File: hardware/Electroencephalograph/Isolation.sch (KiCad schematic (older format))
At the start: 17 parts, among them U4 THI3-0511, U5 ADUM2401BRWZ

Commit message: further routing
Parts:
- added TP14, TP15, TP16, TP8: TestPoint, TestPoint:TestPoint_Pad_D1.0mm, symbol Connector:TestPoint
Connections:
- net CS: now also TP14.1
- net MISO: now also TP8.1
- net MOSI: now also TP15.1
- net SCK: now also TP16.1
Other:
- moved on the sheet: C51
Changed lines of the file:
@@
 Wire Wire Line
 	3100 2600 3100 3200
-Text GLabel 1750 2700 0    50   Input ~ 0
+Text GLabel 1150 2700 0    50   Input ~ 0
 SCK
-Text GLabel 1750 2800 0    50   Input ~ 0
+Text GLabel 1150 2800 0    50   Input ~ 0
 MOSI
-Text GLabel 1750 2900 0    50   Input ~ 0
+Text GLabel 1150 2900 0    50   Input ~ 0
 CS
-Text GLabel 1750 3000 0    50   Output ~ 0
+Text GLabel 1150 3000 0    50   Output ~ 0
 MISO
 Wire Wire Line
-	3150 2700 1750 2700
-Wire Wire Line
-	3150 2800 1750 2800
-Wire Wire Line
-	3150 2900 1750 2900
-Wire Wire Line
-	3150 3000 1750 3000
-Connection ~ 2100 2500
-Wire Wire Line
-	2100 2500 2100 2400
-Wire Wire Line
-	2100 2500 2100 3050
+	3150 2700 2350 2700
+Wire Wire Line
+	3150 2800 2150 2800
+Wire Wire Line
+	3150 2900 1950 2900
+Connection ~ 1500 2500
+Wire Wire Line
+	1500 2500 1500 2400
+Wire Wire Line
+	1500 2500 1500 3050
 $Comp
 L Device:C C?
 U 1 1 5E028BA8
-P 2100 3200
+P 1500 3200
 AR Path="/5DF4CFF8/5E028BA8" Ref="C?"  Part="1"
 AR Path="/5DF61103/5E028BA8" Ref="C?"  Part="1"
 AR Path="/5DFE0AD6/5E028BA8" Ref="C51"  Part="1"
-F 0 "C51" H 2215 3246 50  0000 L CNN
-F 1 "100n" H 2215 3155 50  0000 L CNN
-F 2 "Capacitor_SMD:C_0402_1005Metric" H 2138 3050 50  0001 C CNN
-F 3 "~" H 2100 3200 50  0001 C CNN
-	1    2100 3200
+F 0 "C51" H 1615 3246 50  0000 L CNN
+F 1 "100n" H 1615 3155 50  0000 L CNN
+F 2 "Capacitor_SMD:C_0402_1005Metric" H 1538 3050 50  0001 C CNN
+F 3 "~" H 1500 3200 50  0001 C CNN
+	1    1500 3200
 	-1   0    0    -1
 $EndComp
@@
 L Electroencephalograph:DP_VDD #PWR101
 U 1 1 5E02F433
-P 2100 2400
-F 0 "#PWR101" H 2100 2525 50  0001 C CNN
-F 1 "DP_VDD" H 2117 2573 50  0000 C CNN
-F 2 "" H 2100 2525 50  0001 C CNN
-F 3 "" H 2100 2525 50  0001 C CNN
-	1    2100 2400
+P 1500 2400
+F 0 "#PWR101" H 1500 2525 50  0001 C CNN
+F 1 "DP_VDD" H 1517 2573 50  0000 C CNN
+F 2 "" H 1500 2525 50  0001 C CNN
+F 3 "" H 1500 2525 50  0001 C CNN
+	1    1500 2400
 	1    0    0    -1
 $EndComp
@@
 L Electroencephalograph:DP_GND #PWR102
 U 1 1 5E02EFAB
-P 2100 3400
-F 0 "#PWR102" H 2100 3425 50  0001 C CNN
-F 1 "DP_GND" H 2117 3227 50  0000 C CNN
-F 2 "" H 2100 3425 50  0001 C CNN
-F 3 "" H 2100 3425 50  0001 C CNN
-	1    2100 3400
+P 1500 3400
+F 0 "#PWR102" H 1500 3425 50  0001 C CNN
+F 1 "DP_GND" H 1517 3227 50  0000 C CNN
+F 2 "" H 1500 3425 50  0001 C CNN
+F 3 "" H 1500 3425 50  0001 C CNN
+	1    1500 3400
 	1    0    0    -1
 $EndComp
@@
 $EndComp
 Wire Wire Line
-	2100 3400 2100 3350
+	1500 3400 1500 3350
 Connection ~ 3100 3200
 Wire Wire Line
@@
 	2500 3050 2500 2500
 Wire Wire Line
-	2100 2500 2500 2500
+	1500 2500 2500 2500
 Connection ~ 2500 2500
 Wire Wire Line
@@
 Wire Wire Line
 	4650 2500 5050 2500
+$Comp
+L Connector:TestPoint TP?
+U 1 1 5E2E87E0
+P 2350 2400
+AR Path="/5DF61103/5E2E87E0" Ref="TP?"  Part="1"
+AR Path="/5E142744/5E2E87E0" Ref="TP?"  Part="1"
+AR Path="/5DFE0AD6/5E2E87E0" Ref="TP16"  Part="1"
+F 0 "TP16" V 2304 2588 50  0000 L CNN
+F 1 "TestPoint" V 2395 2588 50  0000 L CNN
+F 2 "TestPoint:TestPoint_Pad_D1.0mm" H 2550 2400 50  0001 C CNN
+F 3 "~" H 2550 2400 50  0001 C CNN
+	1    2350 2400
+	1    0    0    -1
+$EndComp
+$Comp
+L Connector:TestPoint TP?
+U 1 1 5E2E87E6
+P 2150 2400
+AR Path="/5DF61103/5E2E87E6" Ref="TP?"  Part="1"
+AR Path="/5E142744/5E2E87E6" Ref="TP?"  Part="1"
+AR Path="/5DFE0AD6/5E2E87E6" Ref="TP15"  Part="1"
+F 0 "TP15" V 2104 2588 50  0000 L CNN
+F 1 "TestPoint" V 2195 2588 50  0000 L CNN
+F 2 "TestPoint:TestPoint_Pad_D1.0mm" H 2350 2400 50  0001 C CNN
+F 3 "~" H 2350 2400 50  0001 C CNN
+	1    2150 2400
+	1    0    0    -1
+$EndComp
+$Comp
+L Connector:TestPoint TP?
+U 1 1 5E2E87EC
+P 1950 2400
+AR Path="/5DF61103/5E2E87EC" Ref="TP?"  Part="1"
+AR Path="/5E142744/5E2E87EC" Ref="TP?"  Part="1"
+AR Path="/5DFE0AD6/5E2E87EC" Ref="TP14"  Part="1"
+F 0 "TP14" V 1904 2588 50  0000 L CNN
+F 1 "TestPoint" V 1995 2588 50  0000 L CNN
+F 2 "TestPoint:TestPoint_Pad_D1.0mm" H 2150 2400 50  0001 C CNN
+F 3 "~" H 2150 2400 50  0001 C CNN
+	1    1950 2400
+	1    0    0    -1
+$EndComp
+$Comp
+L Connector:TestPoint TP?
+U 1 1 5E2E87F2
+P 1750 2400
+AR Path="/5DF61103/5E2E87F2" Ref="TP?"  Part="1"
+AR Path="/5E142744/5E2E87F2" Ref="TP?"  Part="1"
+AR Path="/5DFE0AD6/5E2E87F2" Ref="TP8"  Part="1"
+F 0 "TP8" V 1704 2588 50  0000 L CNN
+F 1 "TestPoint" V 1795 2588 50  0000 L CNN
+F 2 "TestPoint:TestPoint_Pad_D1.0mm" H 1950 2400 50  0001 C CNN
+F 3 "~" H 1950 2400 50  0001 C CNN
+	1    1750 2400
+	1    0    0    -1
+$EndComp
+Wire Wire Line
+	2350 2400 2350 2700
+Connection ~ 2350 2700
+Wire Wire Line
+	2350 2700 1150 2700
+Wire Wire Line
+	2150 2400 2150 2800
+Connection ~ 2150 2800
+Wire Wire Line
+	2150 2800 1150 2800
+Wire Wire Line
+	1950 2400 1950 2900
+Connection ~ 1950 2900
+Wire Wire Line
+	1950 2900 1150 2900
+Wire Wire Line
+	1750 2400 1750 3000
+Wire Wire Line
+	1150 3000 1750 3000
+Connection ~ 1750 3000
+Wire Wire Line
+	1750 3000 3150 3000
 $EndSCHEMATC

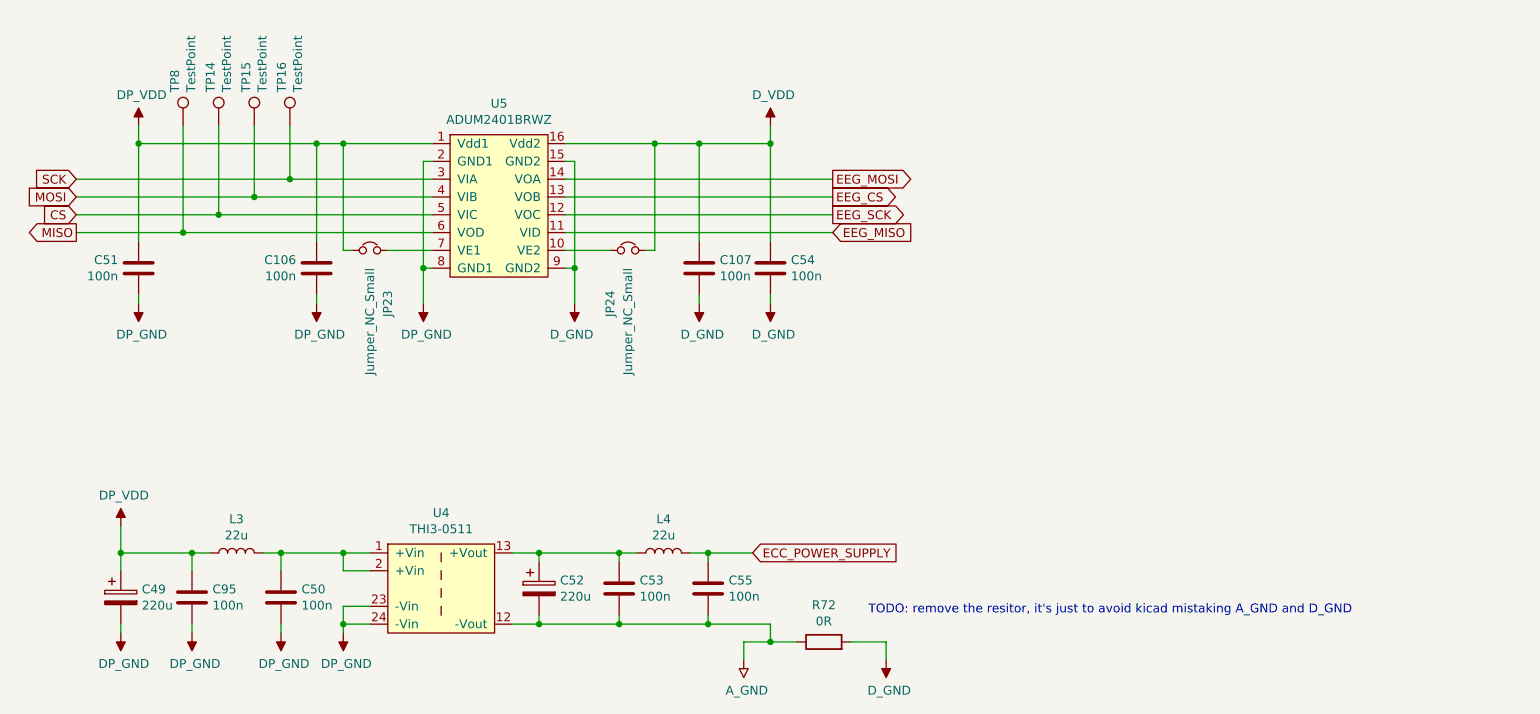
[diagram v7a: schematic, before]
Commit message: fix #41, fix #18
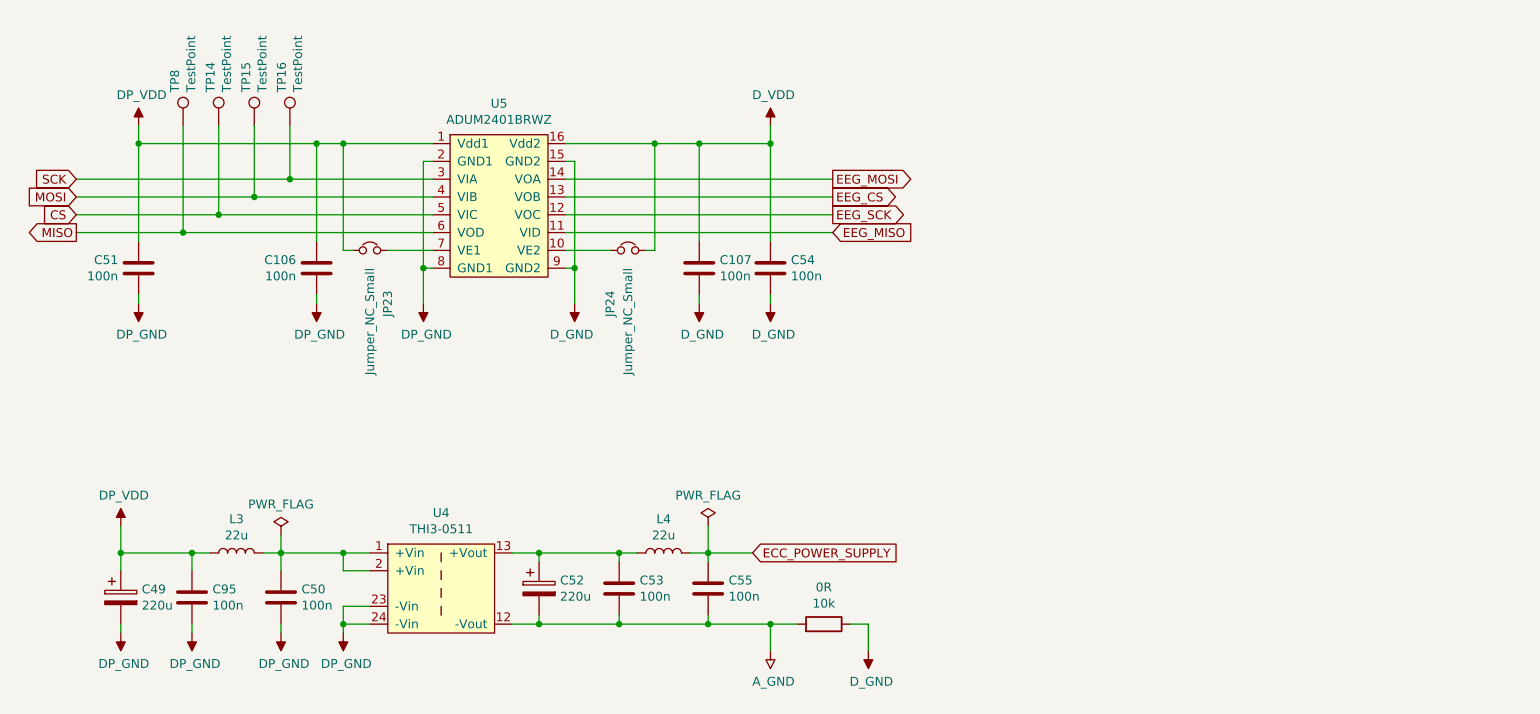
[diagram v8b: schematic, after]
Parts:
- removed R72: 0R, Resistor_SMD:R_0201_0603Metric, symbol Device:R
- added 0R: 10k, Resistor_SMD:R_0402_1005Metric, symbol Device:R
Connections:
- net A_GND: now also 0R.2
- net D_GND: now also 0R.1
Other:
- note removed: "TODO: remove the resitor, it's just to avoid kicad mistaking A_GND and D_GND"
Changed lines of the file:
@@
 $Descr A4 11693 8268
 encoding utf-8
-Sheet 5 8
+Sheet 5 9
 Title "Galvanic isolation"
 Date ""
@@
 L Electroencephalograph:A_GND #PWR108
 U 1 1 5E03B175
-P 4900 5400
-F 0 "#PWR108" H 4900 5425 50  0001 C CNN
-F 1 "A_GND" H 4917 5227 50  0000 C CNN
-F 2 "" H 4900 5425 50  0001 C CNN
-F 3 "" H 4900 5425 50  0001 C CNN
-	1    4900 5400
+P 5050 5350
+F 0 "#PWR108" H 5050 5375 50  0001 C CNN
+F 1 "A_GND" H 5067 5177 50  0000 C CNN
+F 2 "" H 5050 5375 50  0001 C CNN
+F 3 "" H 5050 5375 50  0001 C CNN
+	1    5050 5350
 	1    0    0    -1
 $EndComp
@@
 L Electroencephalograph:D_GND #PWR109
 U 1 1 5E03B5A4
-P 5700 5400
-F 0 "#PWR109" H 5700 5425 50  0001 C CNN
-F 1 "D_GND" H 5717 5227 50  0000 C CNN
-F 2 "" H 5700 5425 50  0001 C CNN
-F 3 "" H 5700 5425 50  0001 C CNN
-	1    5700 5400
+P 5600 5350
+F 0 "#PWR109" H 5600 5375 50  0001 C CNN
+F 1 "D_GND" H 5617 5177 50  0000 C CNN
+F 2 "" H 5600 5375 50  0001 C CNN
+F 3 "" H 5600 5375 50  0001 C CNN
+	1    5600 5350
 	1    0    0    -1
 $EndComp
@@
 	2650 5100 2650 5200
 Wire Wire Line
-	4900 5300 4900 5400
-Wire Wire Line
-	5700 5300 5700 5400
-Wire Wire Line
 	2800 5200 2650 5200
 Wire Wire Line
@@
 Wire Wire Line
 	4700 5200 4700 5150
-Wire Wire Line
-	4700 5200 5050 5200
-Wire Wire Line
-	5050 5200 5050 5300
 Connection ~ 4700 5200
 $Comp
@@
 Wire Wire Line
 	1800 4800 1400 4800
-Wire Wire Line
-	4900 5300 5050 5300
 $Comp
 L Electroencephalograph:DP_GND #PWR177
@@
 Text GLabel 5400 2800 2    50   Output ~ 0
 EEG_CS
-$Comp
-L Device:R R?
-U 1 1 5E15FD88
-P 5350 5300
-AR Path="/5E15FD88" Ref="R?"  Part="1"
-AR Path="/5DF4CFF8/5E15FD88" Ref="R?"  Part="1"
-AR Path="/5DF61103/5E15FD88" Ref="R?"  Part="1"
-AR Path="/5DFE0AD6/5E15FD88" Ref="R72"  Part="1"
-F 0 "R72" V 5557 5300 50  0000 C CNN
-F 1 "0R" V 5466 5300 50  0000 C CNN
-F 2 "Resistor_SMD:R_0201_0603Metric" V 5280 5300 50  0001 C CNN
-F 3 "~" H 5350 5300 50  0001 C CNN
-	1    5350 5300
-	0    -1   -1   0
-$EndComp
-Wire Wire Line
-	5050 5300 5200 5300
-Connection ~ 5050 5300
-Wire Wire Line
-	5500 5300 5700 5300
-Text Notes 5600 5150 0    50   ~ 0
-TODO: remove the resitor, it's just to avoid kicad mistaking A_GND and D_GND
 $Comp
 L Device:C C?
@@
 Wire Wire Line
 	1750 3000 3150 3000
+Wire Wire Line
+	5600 5200 5600 5350
+Wire Wire Line
+	4700 5200 5050 5200
+Wire Wire Line
+	5050 5350 5050 5200
+$Comp
+L power:PWR_FLAG #FLG0101
+U 1 1 5ECF772F
+P 2300 4700
+F 0 "#FLG0101" H 2300 4775 50  0001 C CNN
+F 1 "PWR_FLAG" H 2300 4873 50  0000 C CNN
+F 2 "" H 2300 4700 50  0001 C CNN
+F 3 "~" H 2300 4700 50  0001 C CNN
+	1    2300 4700
+	1    0    0    -1
+$EndComp
+Wire Wire Line
+	2300 4800 2300 4700
+$Comp
+L power:PWR_FLAG #FLG0104
+U 1 1 5ED49BA7
+P 4700 4650
+F 0 "#FLG0104" H 4700 4725 50  0001 C CNN
+F 1 "PWR_FLAG" H 4700 4823 50  0000 C CNN
+F 2 "" H 4700 4650 50  0001 C CNN
+F 3 "~" H 4700 4650 50  0001 C CNN
+	1    4700 4650
+	1    0    0    -1
+$EndComp
+Wire Wire Line
+	4700 4800 4700 4650
+$Comp
+L Device:R R?
+U 1 1 5EC9AC63
+P 5350 5200
+AR Path="/5EC9AC63" Ref="R?"  Part="1"
+AR Path="/5DAEEEF4/5EC9AC63" Ref="R?"  Part="1"
+AR Path="/5DD5C7F6/5EC9AC63" Ref="R?"  Part="1"
+AR Path="/5E142744/5EC9AC63" Ref="R?"  Part="1"
+AR Path="/5DFE0AD6/5EC9AC63" Ref="0R"  Part="1"
+F 0 "0R" V 5557 5200 50  0000 C CNN
+F 1 "10k" V 5466 5200 50  0000 C CNN
+F 2 "Resistor_SMD:R_0402_1005Metric" V 5280 5200 50  0001 C CNN
+F 3 "~" H 5350 5200 50  0001 C CNN
+	1    5350 5200
+	0    1    -1   0
+$EndComp
+Wire Wire Line
+	5050 5200 5200 5200
+Connection ~ 5050 5200
+Wire Wire Line
+	5500 5200 5600 5200
 $EndSCHEMATC
